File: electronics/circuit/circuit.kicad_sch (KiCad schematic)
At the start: 27 parts, among them J1 PWR, J2 debugWIRE, J3 ESP8266, J4 Motor2, J5 Motor1, J6 Motor3, Q1 BSS138, Q2 BSS138, SW1 SW_RESET, U1 LD1117V33, U2 ATtiny84A-P, U3 SN74HC595N, U4 SN74HC595N

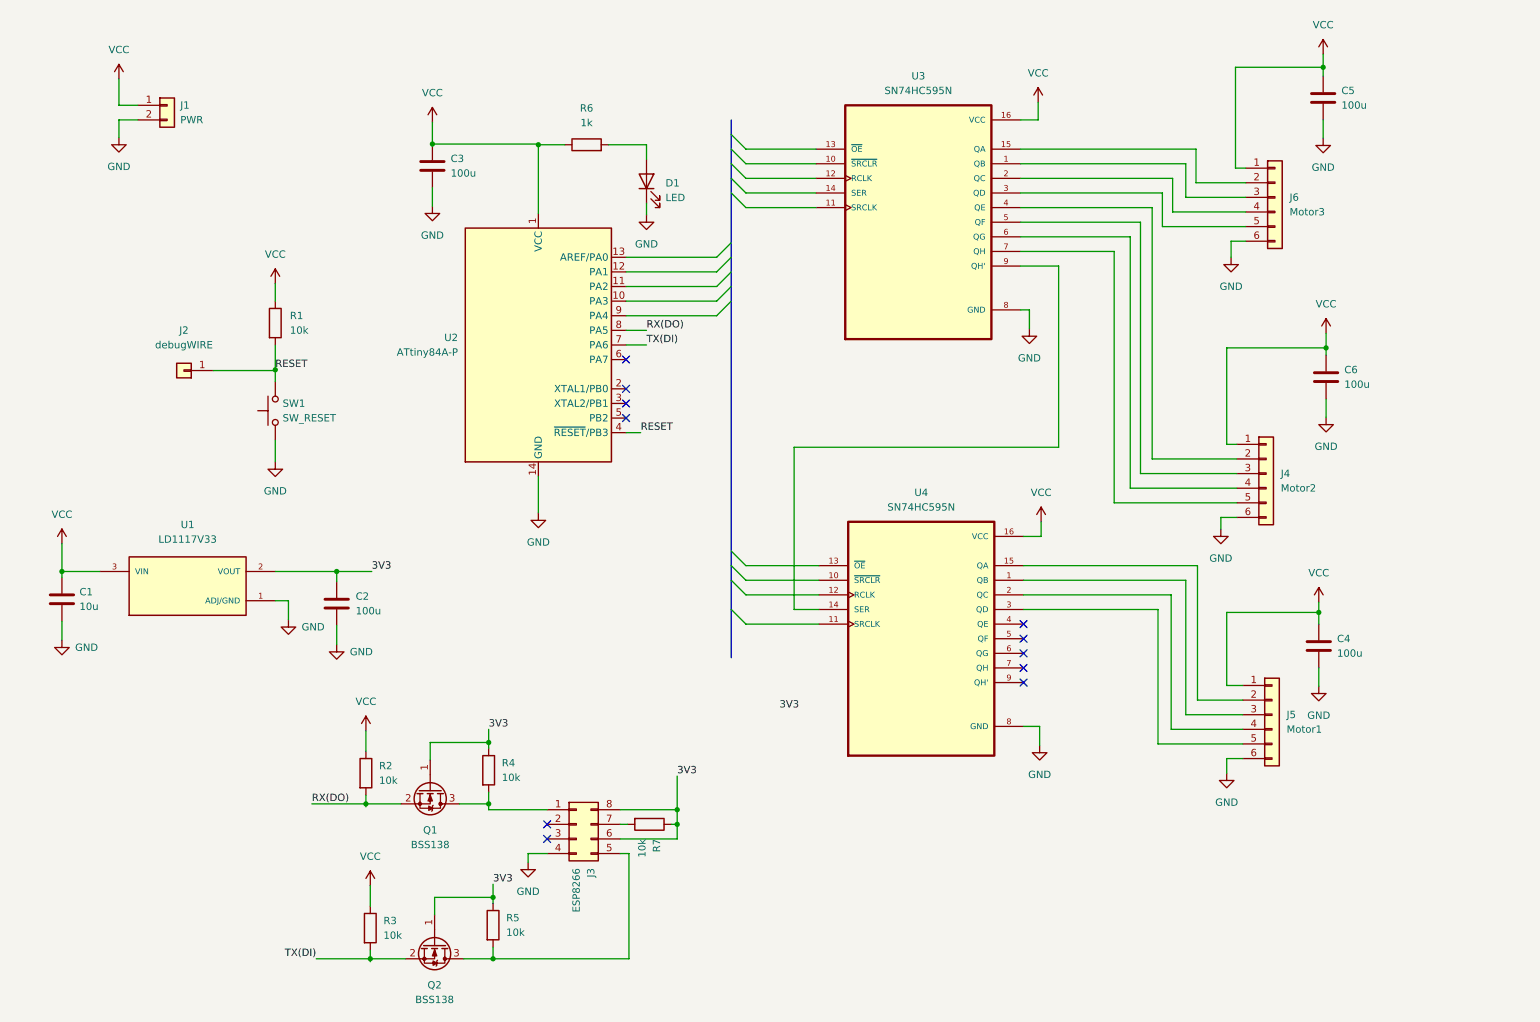
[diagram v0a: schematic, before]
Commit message: Finish USI Half Duplex UART library
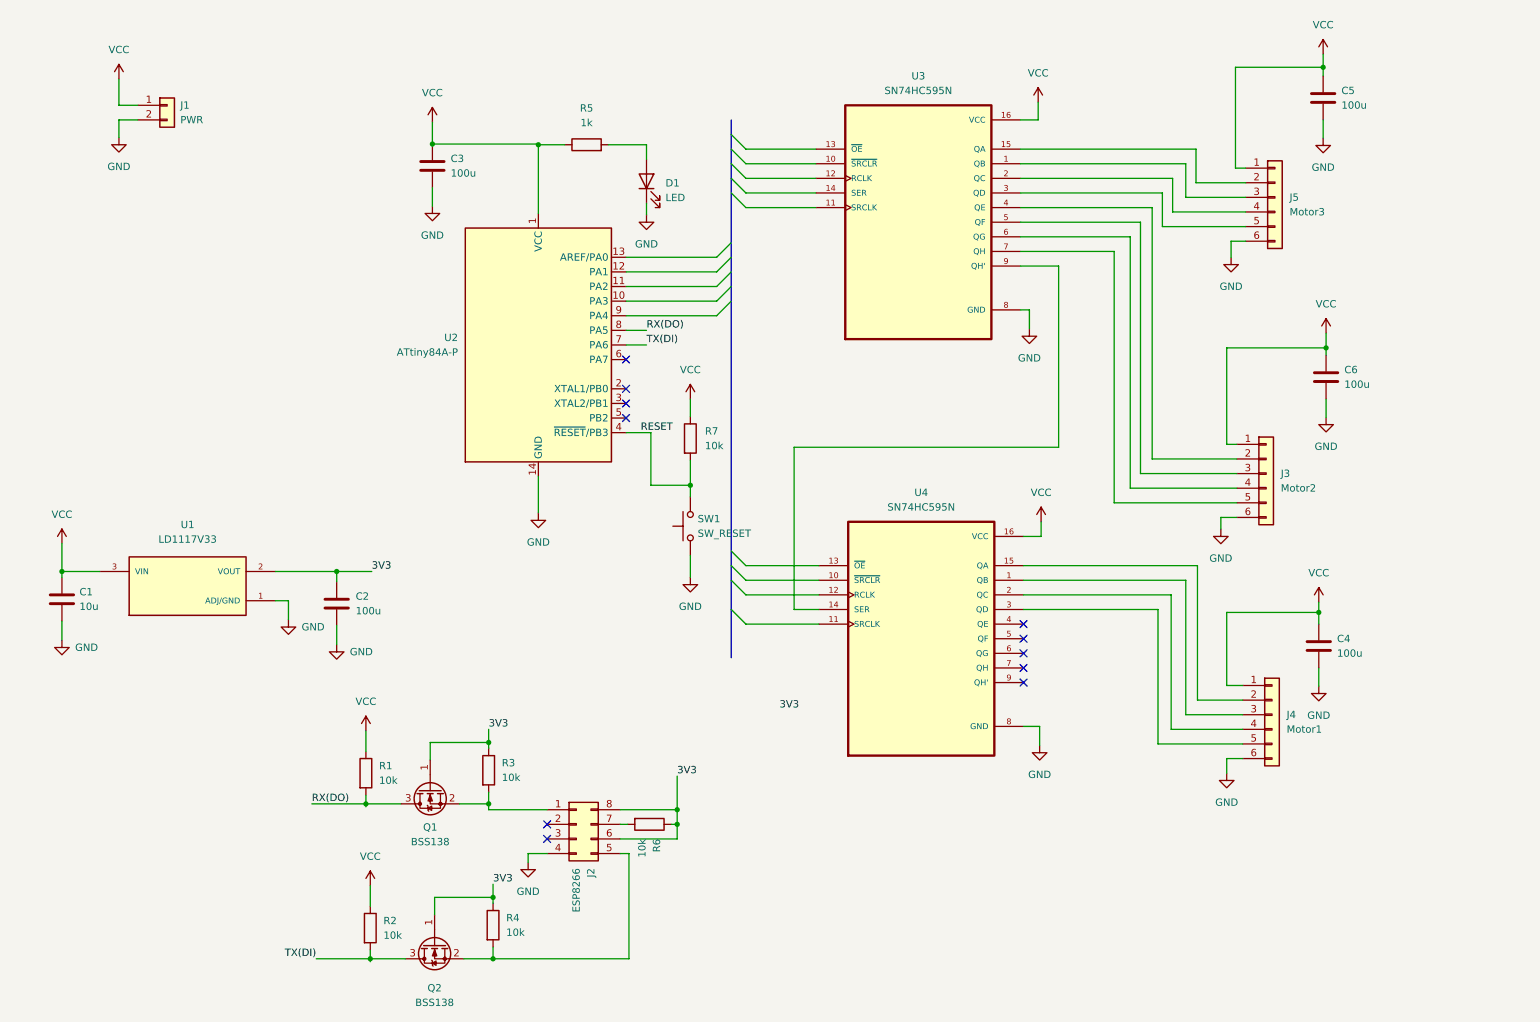
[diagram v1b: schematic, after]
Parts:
- removed J2: debugWIRE, symbol Connector_Generic:Conn_01x01
- removed R1: 10k, symbol Device:R
- added R7: 10k, symbol Device:R
- renumbered J3 to J2, J4 to J3, J5 to J4, J6 to J5, R2 to R1, R3 to R2, R4 to R3, R5 to R4, R6 to R5, R7 to R6
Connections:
- net RESET: now also R7.2
- net RX(DO): now also Q1.3 (D); no longer Q1.2 (S)
- net TX(DI): now also Q2.3 (D); no longer Q2.2 (S)
- net VCC: now also R7.1
- net at J2.5 (Pin_5), R4.2: now also Q2.2 (S); no longer Q2.3 (D)
- net at J2.1 (Pin_1), R3.2: now also Q1.2 (S); no longer Q1.3 (D)
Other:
- moved on the sheet: Q1, Q2

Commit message: Update schematic with IR sensors
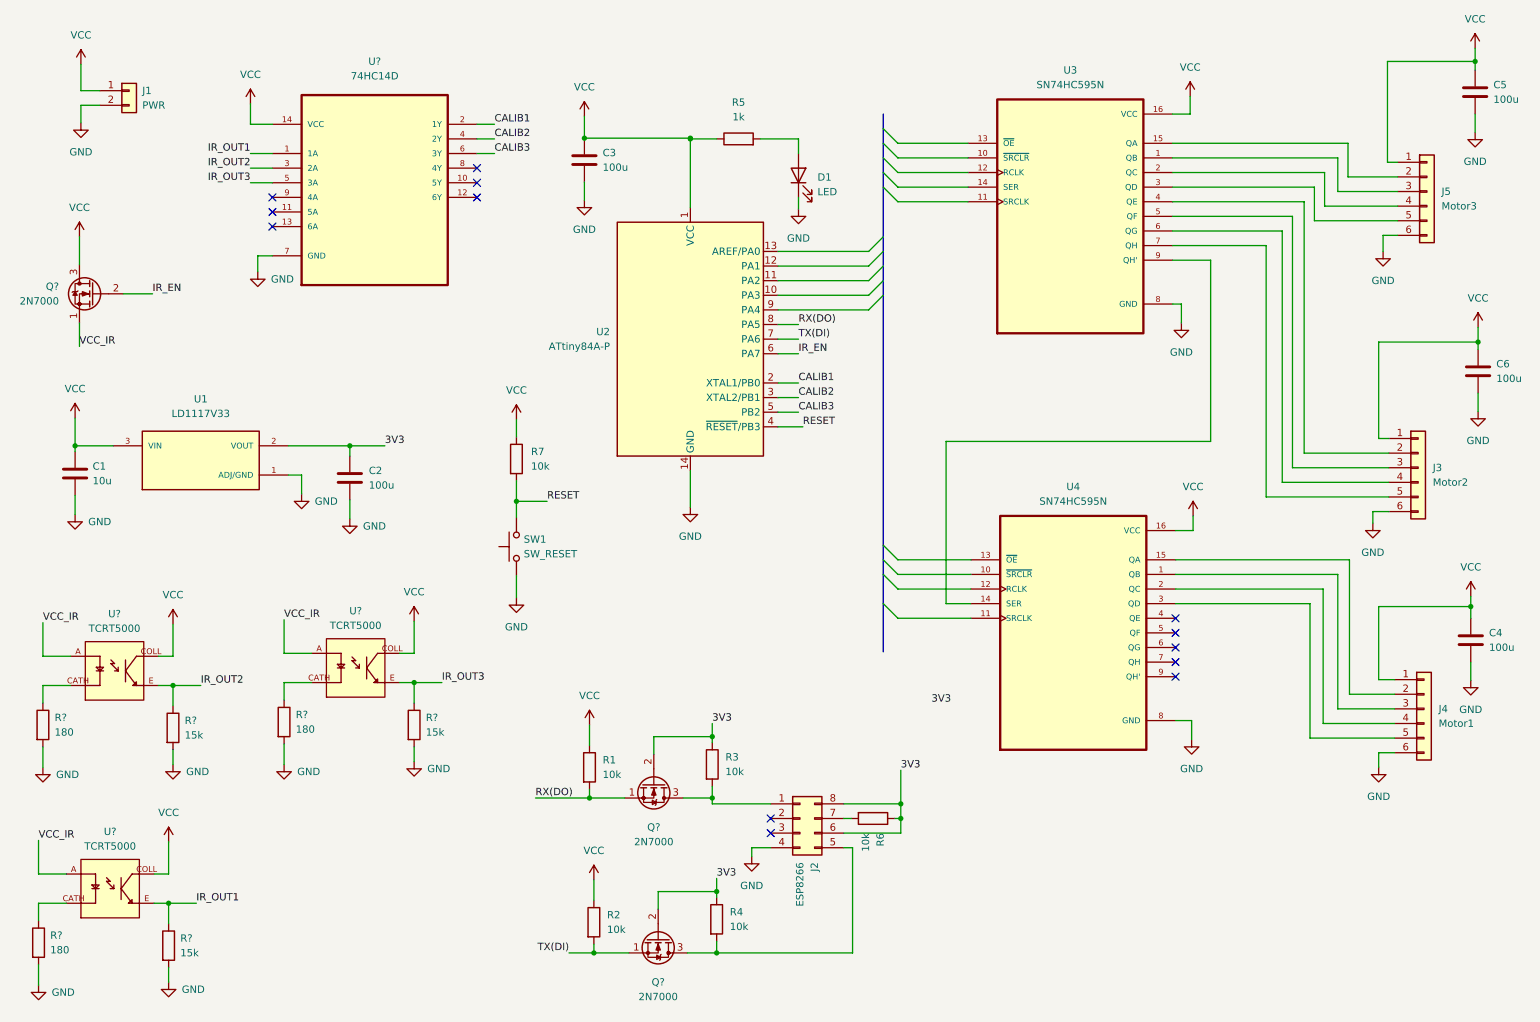
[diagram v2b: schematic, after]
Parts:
- removed Q1, Q2: BSS138, Package_TO_SOT_SMD:SOT-23, symbol Transistor_FET:BSS138
- added Q? (x3): 2N7000, Package_TO_SOT_THT:TO-92_Inline, symbol Transistor_FET:2N7000
- added R? (x3): 15k, symbol Device:R
- added R? (x3): 180, symbol Device:R
- added U? (x3): TCRT5000, OPTO_TCRT5000, symbol IR Sensor:TCRT5000
- added U?: 74HC14D, SOIC127P600X175-14N, symbol Inverter IC:74HC14D
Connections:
- net 3V3: now also Q?.2 (G), Q?.2 (G)
- net GND: now also R?.2, R?.2, R?.2, R?.2, R?.2, R?.2, U?.7 (GND)
- net RESET: now also SW1.2
- net RX(DO): now also Q?.1 (S)
- net TX(DI): now also Q?.1 (S)
- net VCC: now also Q?.3 (D), U?.14 (VCC), U?.COLL, U?.COLL, U?.COLL
- net at J2.5 (Pin_5), R4.2: now also Q?.3 (D)
- net at J2.1 (Pin_1), R3.2: now also Q?.3 (D)
- net CALIB1: now reaches U2.2 (XTAL1/PB0)
- net CALIB1: now also U?.2 (1Y)
- net CALIB2: now reaches U2.3 (XTAL2/PB1)
- net CALIB2: now also U?.4 (2Y)
- net CALIB3: now reaches U2.5 (PB2)
- net CALIB3: now also U?.6 (3Y)
- net IR_EN: now reaches U2.6 (PA7)
- net IR_EN: now also Q?.2 (G)
- new net: R?.1, U?.CATH (x3)
- new net IR_OUT1: R?.1, U?.1 (1A), U?.E
- new net IR_OUT2: R?.1, U?.3 (2A), U?.E
- new net IR_OUT3: R?.1, U?.5 (3A), U?.E
- new net VCC_IR: Q?.1 (S), U?.A, U?.A, U?.A
- no-connect marks 11 -> 13
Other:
- moved on the sheet: C1, C2, C3, C4, C5, C6, D1, J1, J2, J3, J4, J5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

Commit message: Create shift register driver
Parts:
- gave numbers to parts that had none: 13
- renumbered R3 to R10, R4 to R11, R5 to R12, R6 to R13, R1 to R8, R2 to R9, U1 to U3, U2 to U6, U3 to U7, U4 to U8
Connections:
- net RX(DO): now also Q2.3 (D); no longer Q2.1 (S)
- net TX(DI): now also Q3.3 (D); no longer Q3.1 (S)
- net at J2.5 (Pin_5), R11.2: now also Q3.1 (S); no longer Q3.3 (D)
- net at J2.1 (Pin_1), R10.2: now also Q2.1 (S); no longer Q2.3 (D)
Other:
- moved on the sheet: Q2, Q3
